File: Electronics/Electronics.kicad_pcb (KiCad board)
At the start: 2 copper layers, 43 parts, among them J1 Conn_01x04, J2 Conn_02x08_Counter_Clockwise, J3 Terminal1x2, J4 Terminal1x2, J5 Terminal1x2, J6 Terminal1x2, J7 Terminal1x2, K1 G3MB-202P, K2 G3MB-202P, K3 G3MB-202P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

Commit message: finished PCB layout
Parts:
- removed J2: Conn_02x08_Counter_Clockwise, Package_DIP:DIP-16_W7.62mm_Socket_LongPads
- added C10: 10nF, Capacitor_THT:C_Disc_D5.0mm_W2.5mm_P2.50mm, F.Cu at (138.6, 114.5)
- added C7: 10nF, Capacitor_THT:C_Disc_D5.0mm_W2.5mm_P2.50mm, F.Cu at (112.7, 114.5)
- added C8: 10nF, Capacitor_THT:C_Disc_D5.0mm_W2.5mm_P2.50mm, F.Cu at (121.4, 114.5)
- added C9: 10nF, Capacitor_THT:C_Disc_D5.0mm_W2.5mm_P2.50mm, F.Cu at (130.0, 114.5)
- added H1: MountingHole, MountingHole:MountingHole_2.7mm_Pad, F.Cu at (109.9, 72.6)
- added H2: MountingHole, MountingHole:MountingHole_2.7mm_Pad, F.Cu at (208.7, 72.4)
- added H3: MountingHole, MountingHole:MountingHole_2.7mm_Pad, F.Cu at (106.6, 129.1)
- added STC8H8K64U1: SOP16_Breakout, Module:Pololu_Breakout-16_15.2x20.3mm, F.Cu at (150.6, 93.4)
- CP2102_TTL_Converter1: renamed from J1; value Conn_01x04 -> PinHeader1x4; footprint Connector_JST:JST_EH_S4B-EH_1x04_P2.50mm_Horizontal -> Connector_PinSocket_2.54mm:PinSocket_1x04_P2.54mm_Vertical
- PS1: value HLK-2M05 -> HLK-5M05; footprint Converter_ACDC:Converter_ACDC_Hi-Link_HLK-2Mxx -> Converter_ACDC:Converter_ACDC_Hi-Link_HLK-5Mxx
- R1: value 10k -> 75
- R10, R11, R8, R9: value 10k -> 330
- R12: value 10k -> 1k
- R13, R6: value 10k -> 220
- R2, R3, R4, R5: value 10k -> 470
- moved J7 74.3 mm to (204.6, 129.6)
- moved PRGB_LED4 71.4 mm to (139.9, 119.4)
- moved PRGB_LED1 71.4 mm to (114.0, 119.4)
- moved PRGB_LED2 71.4 mm to (122.6, 119.4)
- moved PRGB_LED3 71.4 mm to (131.3, 119.4)
- moved BZ1 68.9 mm to (125.4, 107.2), turned to 90 degrees
- moved U5 66.6 mm to (111.3, 102.3), turned to -90 degrees
- moved J5 65.3 mm to (156.8, 129.5), turned to 180 degrees
- moved R1 59.4 mm to (117.4, 103.2), turned to -90 degrees
- moved J6 59.1 mm to (167.4, 129.5), turned to 180 degrees
- moved R13 58.1 mm to (114.4, 97.9), turned to 180 degrees
- moved J3 57.6 mm to (188.8, 129.5), turned to 180 degrees
- moved J4 56.4 mm to (178.1, 129.5), turned to 180 degrees
- moved PS1 46.2 mm to (198.7, 116.3), turned to 90 degrees
- moved K4 45.5 mm to (157.4, 107.6), turned to -90 degrees
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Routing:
- net +5VA: track 0.00 -> 128.2 mm
- net GND1: track 58.8 -> 166.0 mm
- net GND2: track 154.9 -> 257.2 mm
- net Relay1: track 0.00 -> 54.3 mm
- net Relay2: track 0.00 -> 45.8 mm
- net +5VD: track 159.4 -> 200.1 mm
- net Relay4: track 0.00 -> 37.4 mm
- net Relay3: track 0.00 -> 31.6 mm
- net PRGB_DATA: track 0.00 -> 25.4 mm
- net STC_RX: track 0.00 -> 16.2 mm
- net Net-(J7-Pin_2): track 0.00 -> 13.7 mm
- net Net-(J7-Pin_1): track 0.00 -> 13.4 mm
- net Net-(PRGB_LED1-DIN): track 6.51 -> 16.2 mm
- net Buzzer: track 0.00 -> 9.23 mm
- net STC_TX: track 0.00 -> 8.95 mm
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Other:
- board outline added: 113.3 x 67.5 mm

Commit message: added a force anchor hole for the PCB
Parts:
- added H4: MountingHole, MountingHole:MountingHole_2.7mm_Pad, F.Cu at (211.1, 128.6)
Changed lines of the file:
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@@
 		)
+	)
+	(footprint "MountingHole:MountingHole_2.7mm_Pad"
+		(layer "F.Cu")
+		(at 211.1 128.6)
+		(descr "Mounting Hole 2.7mm")
+		(tags "mounting hole 2.7mm")
+		(property "Reference" "H4"
+			(at 0 -3.7 0)
+			(layer "F.SilkS")
+			(effects
+				(font
+					(size 1 1)
+					(thickness 0.15)
+				)
+			)
+		)
+		(property "Value" "MountingHole"
+			(at -1.7 -5.3 0)
+			(layer "F.Fab")
+			(effects
+				(font
+					(size 1 1)
+					(thickness 0.15)
+				)
+			)
+		)
+		(property "Datasheet" ""
+			(at 0 0 0)
+			(unlocked yes)
+			(layer "F.Fab")
+			(hide yes)
+			(effects
+				(font
+					(size 1.27 1.27)
+					(thickness 0.15)
+				)
+			)
+		)
+		(property "Description" "Mounting Hole without connection"
+			(at 0 0 0)
+			(unlocked yes)
+			(layer "F.Fab")
+			(hide yes)
+			(effects
+				(font
+					(size 1.27 1.27)
+					(thickness 0.15)
+				)
+			)
+		)
+		(property ki_fp_filters "MountingHole*")
+		(sheetname "/")
+		(sheetfile "Electronics.kicad_sch")
+		(attr exclude_from_pos_files exclude_from_bom)
+		(fp_circle
+			(center 0 0)
+			(end 2.7 0)
+			(stroke
+				(width 0.15)
+				(type solid)
+			)
+			(fill no)
+			(layer "Cmts.User")
+		)
+		(fp_circle
+			(center 0 0)
+			(end 2.95 0)
+			(stroke
+				(width 0.05)
+				(type solid)
+			)
+			(fill no)
+			(layer "F.CrtYd")
+		)
+		(fp_text user "${REFERENCE}"
+			(at 0 0 0)
+			(layer "F.Fab")
+			(effects
+				(font
+					(size 1 1)
+					(thickness 0.15)
+				)
+			)
+		)
+		(pad "1" thru_hole circle
+			(at 0 0)
+			(size 5.4 5.4)
+			(drill 2.7)
+			(layers "*.Cu" "*.Mask")
+			(remove_unused_layers no)
+		)
+		(embedded_fonts no)
 	)
 	(footprint "Capacitor_THT:C_Disc_D5.0mm_W2.5mm_P2.50mm"

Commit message: started 3D modelling enclosure
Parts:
- moved J4 5.12 mm to (173.0, 129.5), turned to 0 degrees
- moved J3 5.12 mm to (183.6, 129.5), turned to 0 degrees
- moved J6 5.12 mm to (162.3, 129.5), turned to 0 degrees
- moved J5 5.00 mm to (151.8, 129.5), turned to 0 degrees
- moved J7 5.00 mm to (199.6, 129.5), turned to 0 degrees
- moved K1 0.05 mm to (182.3, 107.6)
- moved K2 0.05 mm to (174.1, 107.6)
- moved K3 0.05 mm to (165.8, 107.6)
- moved K4 0.05 mm to (157.5, 107.6)
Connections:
- K1 pad 1: Net-(J3-Pin_2) -> Net-(J3-Pin_1)
- K1 pad 2: Net-(J3-Pin_1) -> Net-(J3-Pin_2)
- K2 pad 1: Net-(J4-Pin_2) -> Net-(J4-Pin_1)
- K2 pad 2: Net-(J4-Pin_1) -> Net-(J4-Pin_2)
- K3 pad 1: Net-(J6-Pin_2) -> Net-(J6-Pin_1)
- K3 pad 2: Net-(J6-Pin_1) -> Net-(J6-Pin_2)
- K4 pad 1: Net-(J5-Pin_2) -> Net-(J5-Pin_1)
- K4 pad 2: Net-(J5-Pin_1) -> Net-(J5-Pin_2)
- PS1 pad 1: Net-(J7-Pin_2) -> Net-(J7-Pin_1)
- PS1 pad 2: Net-(J7-Pin_1) -> Net-(J7-Pin_2)
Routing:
- net Net-(J3-Pin_2): track 12.9 -> 22.7 mm
- net Net-(J3-Pin_1): track 22.7 -> 12.9 mm
- net Net-(J4-Pin_2): track 11.9 -> 21.7 mm
- net Net-(J4-Pin_1): track 21.7 -> 11.9 mm
- net Net-(J5-Pin_2): track 13.5 -> 21.8 mm
- net Net-(J5-Pin_1): track 21.8 -> 13.5 mm
- net Net-(J6-Pin_2): track 12.6 -> 20.7 mm
- net Net-(J6-Pin_1): track 20.7 -> 12.6 mm

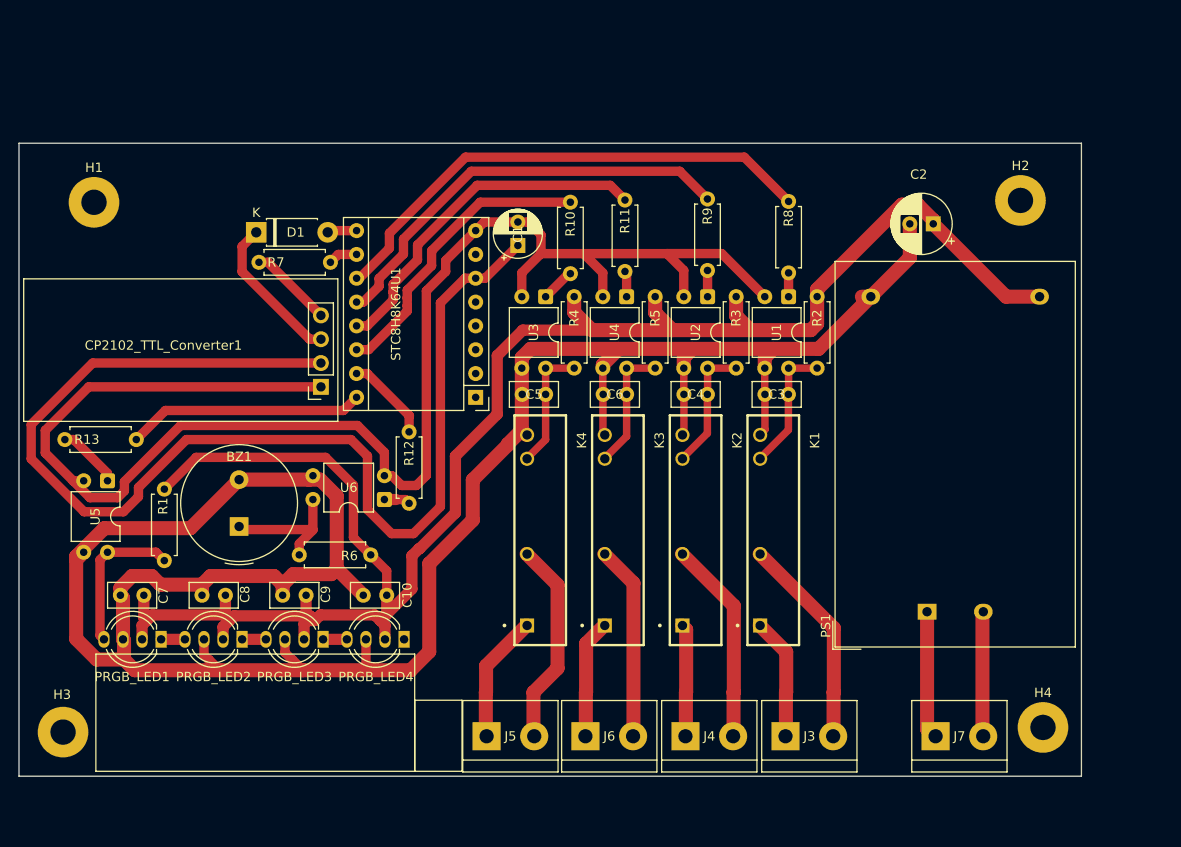
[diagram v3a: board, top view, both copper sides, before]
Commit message: added schematic and PCB layout for mechanical relays
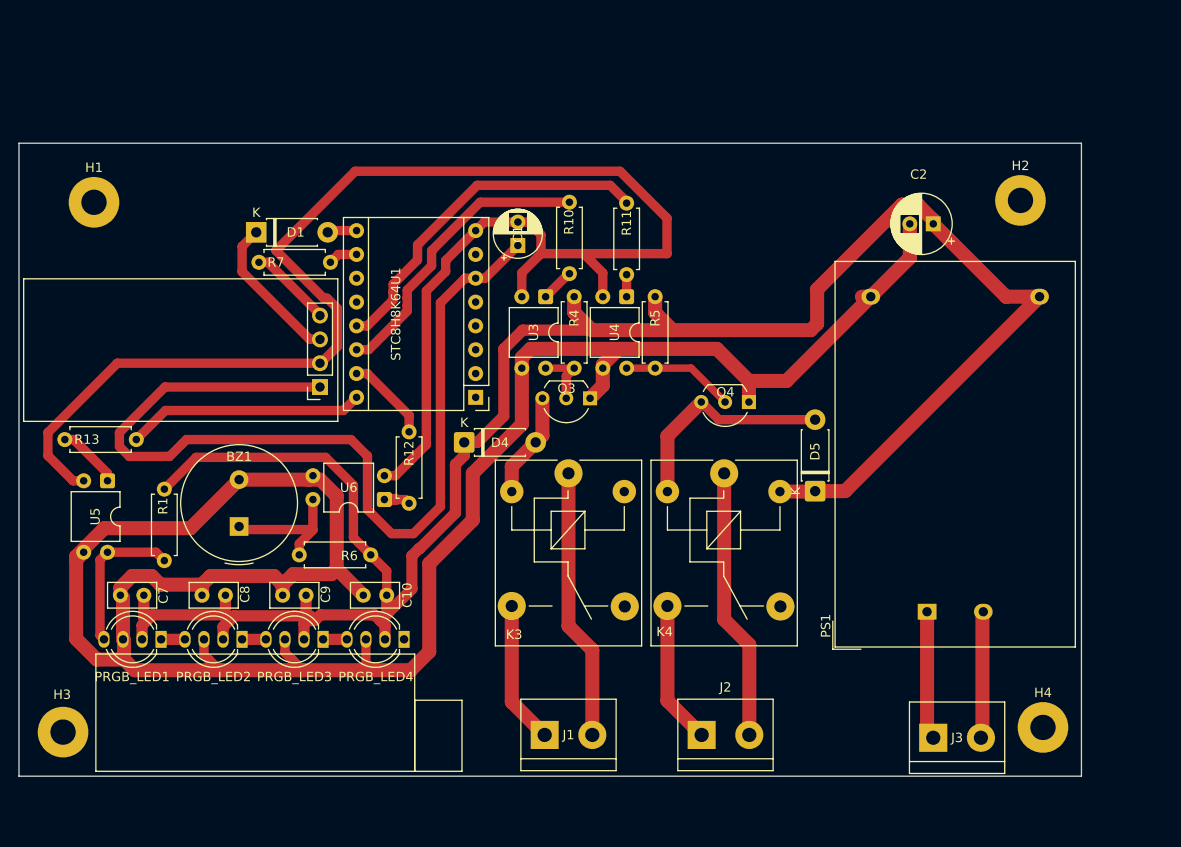
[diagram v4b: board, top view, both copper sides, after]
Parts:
- removed C3, C4, C5, C6: 10nF, Capacitor_THT:C_Disc_D5.0mm_W2.5mm_P2.50mm
- removed J4, J5, J6, J7: Terminal1x2, TerminalBlock:TerminalBlock_bornier-2_P5.08mm
- removed K1, K2: G3MB-202P, G3MB-202P:RELAY_G3MB-202P
- removed R2, R3: 470, Resistor_THT:R_Axial_DIN0207_L6.3mm_D2.5mm_P7.62mm_Horizontal
- removed R8, R9: 330, Resistor_THT:R_Axial_DIN0207_L6.3mm_D2.5mm_P7.62mm_Horizontal
- removed U1, U2: PC817, Package_DIP:DIP-4_W7.62mm
- added D4: 1N5817, Diode_THT:D_DO-41_SOD81_P7.62mm_Horizontal, F.Cu at (149.4, 98.2)
- added D5: 1N5817, Diode_THT:D_DO-41_SOD81_P7.62mm_Horizontal, F.Cu at (186.8, 103.4)
- added J1: Terminal1x2, TerminalBlock:TerminalBlock_bornier-2_P5.08mm, F.Cu at (158.0, 129.4)
- added J2: Terminal1x2, TerminalBlock:TerminalBlock_bornier-2_P5.08mm, F.Cu at (174.7, 129.4)
- added Q3: S8050, Package_TO_SOT_THT:TO-92_Inline_Wide, F.Cu at (162.8, 93.5)
- added Q4: S8050, Package_TO_SOT_THT:TO-92_Inline_Wide, F.Cu at (179.7, 93.9)
- K3, K4: value G3MB-202P -> Relay; footprint G3MB-202P:RELAY_G3MB-202P -> Relay_THT:Relay_SPDT_SANYOU_SRD_Series_Form_C
- moved K4 20.5 mm to (177.1, 101.5)
- moved J3 15.8 mm to (199.4, 129.7)
- moved K3 8.04 mm to (160.5, 101.5)
- moved R11 0.38 mm to (166.7, 72.7)
- moved CP2102_TTL_Converter1 0.10 mm to (134.0, 92.3)
- moved R10 0.10 mm to (160.6, 72.6)
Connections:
- CP2102_TTL_Converter1 pad 1: GND1 -> +5VA
- CP2102_TTL_Converter1 pad 2: +5VA -> GND1
- K3 pad 3: Net-(C6-Pad1) -> Net-(J1-Pin_1)
- K3 pad 4: GND2 -> unconnected-(K3-Pad4)
- K4 pad 3: Net-(C5-Pad1) -> Net-(J2-Pin_1)
- K4 pad 4: GND2 -> unconnected-(K4-Pad4)
- PS1 pad 1: Net-(J7-Pin_1) -> Net-(J3-Pin_1)
- PS1 pad 2: Net-(J7-Pin_2) -> Net-(J3-Pin_2)
- R4 pad 2: Net-(C5-Pad1) -> Net-(Q3-B)
- R5 pad 2: Net-(C6-Pad1) -> Net-(Q4-B)
- STC8H8K64U1 pad 11: Relay1 -> unconnected-(STC8H8K64U1-Pin_11-Pad11)
- STC8H8K64U1 pad 12: Relay2 -> unconnected-(STC8H8K64U1-Pin_12-Pad12)
- U3 pad 4: Net-(C5-Pad1) -> Net-(Q3-B)
- U4 pad 4: Net-(C6-Pad1) -> Net-(Q4-B)
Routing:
- net Relay1: track 54.3 -> 0.00 mm
- net Relay2: track 45.8 -> 0.00 mm
- net +5VD: track 200.1 -> 233.1 mm
- net +5VA: track 128.2 -> 101.5 mm
- net Net-(J4-Pin_2): track 21.7 -> 0.00 mm
- net GND2: track 257.2 -> 238.7 mm
- net Net-(J1-Pin_2): track 12.6 -> 29.0 mm
- net Net-(J2-Pin_2): track 13.5 -> 29.0 mm
- net Net-(J2-Pin_1): track 0.00 -> 15.3 mm
- net Net-(J1-Pin_1): track 0.00 -> 15.2 mm
- net Net-(C3-Pad1): track 14.0 -> 0.00 mm
- net Net-(C4-Pad1): track 13.8 -> 0.00 mm
- net Net-(C6-Pad1): track 13.7 -> 0.00 mm
- net Net-(J7-Pin_1): track 13.7 -> 0.00 mm
- net Net-(C5-Pad1): track 13.5 -> 0.00 mm
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
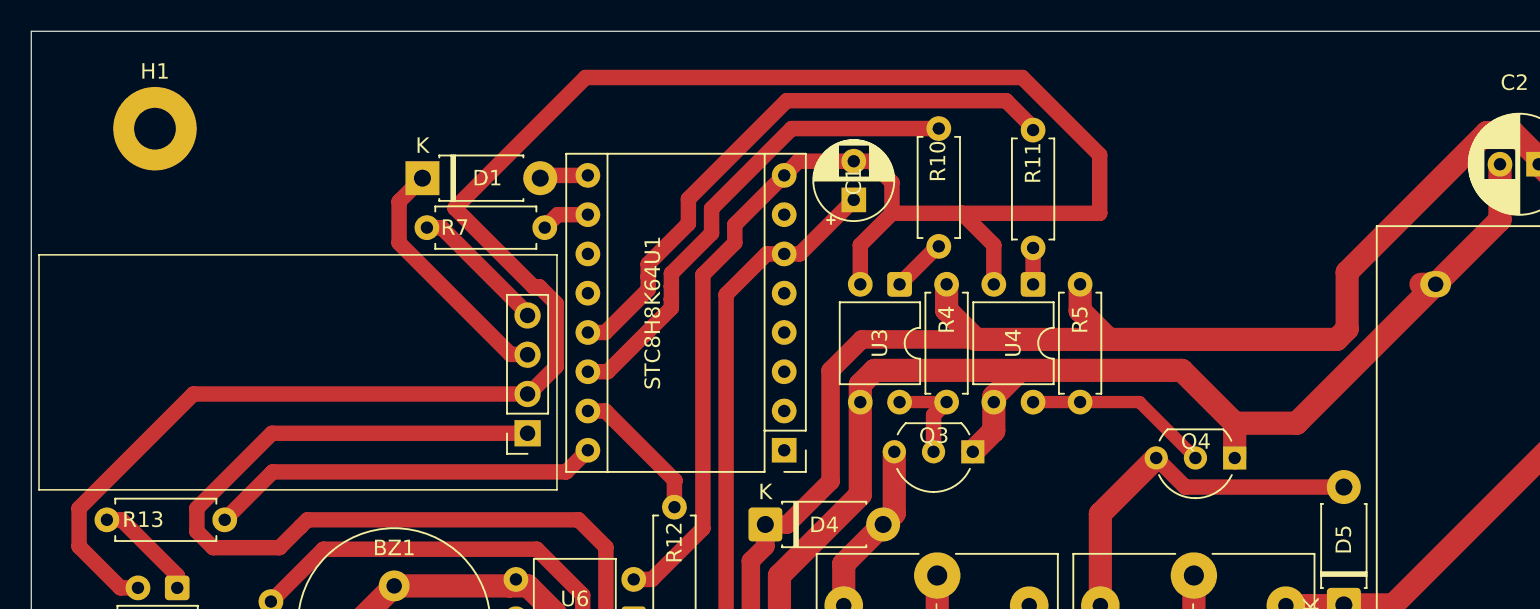
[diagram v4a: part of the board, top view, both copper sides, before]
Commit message: added temperature sensor and AC detect schematic and PCB layout
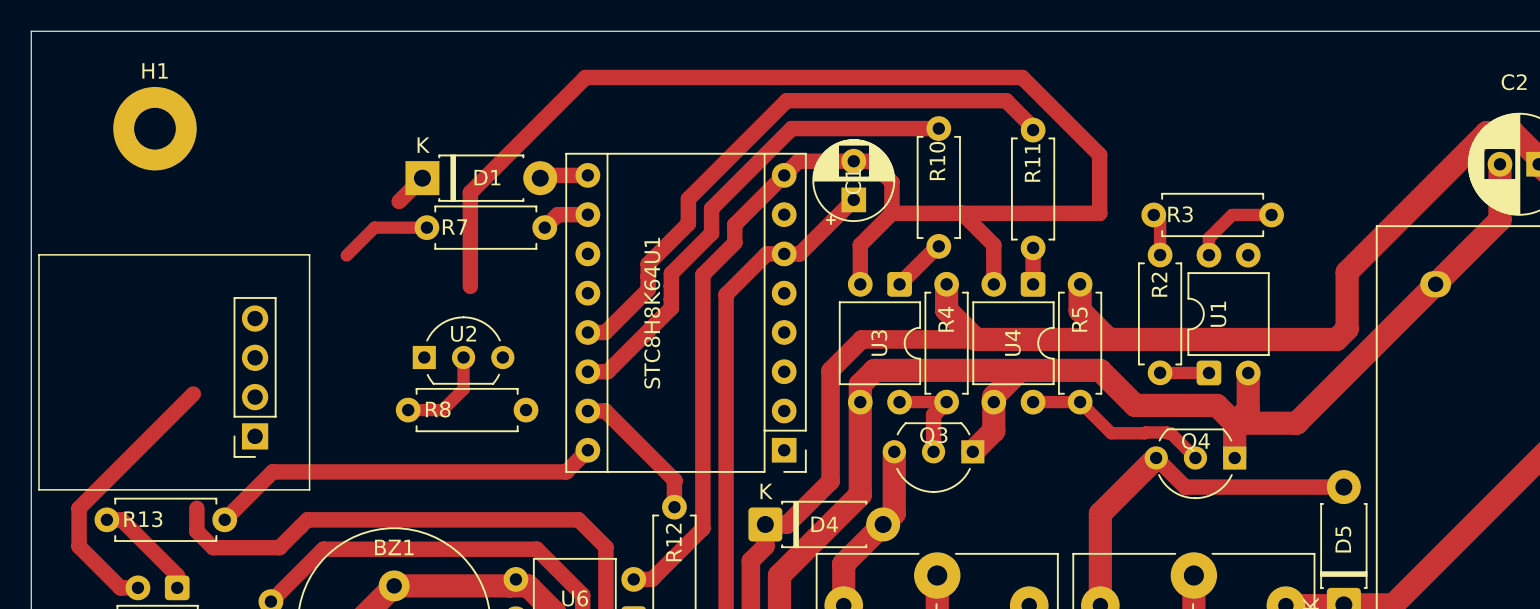
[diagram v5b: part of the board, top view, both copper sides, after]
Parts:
- added R2: 330, Resistor_THT:R_Axial_DIN0207_L6.3mm_D2.5mm_P7.62mm_Horizontal, F.Cu at (174.9, 80.8)
- added R3: 10k, Resistor_THT:R_Axial_DIN0207_L6.3mm_D2.5mm_P7.62mm_Horizontal, F.Cu at (174.5, 78.2)
- added R8: 2k, Resistor_THT:R_Axial_DIN0207_L6.3mm_D2.5mm_P7.62mm_Horizontal, F.Cu at (126.3, 90.8)
- added U1: PC817, Package_DIP:DIP-4_W7.62mm, F.Cu at (178.1, 88.4)
- added U2: LM35-LP, Package_TO_SOT_THT:TO-92L_Inline_Wide, F.Cu at (127.3, 87.4)
- moved CP2102_TTL_Converter1 17.6 mm to (116.4, 92.5)
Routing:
- net GND1: track 171.4 -> 138.6 mm
- net +5VA: track 101.5 -> 78.1 mm
- net STC_RX: track 16.2 -> 2.14 mm
- net Net-(U2-V_{OUT}): track 0.00 -> 6.19 mm
- net AC_STATE: track 0.00 -> 5.77 mm
- net Net-(R2-Pad2): track 0.00 -> 3.16 mm
- net STC_TX: track 8.95 -> 5.94 mm
- net +5VD: track 233.1 -> 235.8 mm
- net GND2: track 238.7 -> 241.4 mm
